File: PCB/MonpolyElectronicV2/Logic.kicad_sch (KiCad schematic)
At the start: 2 parts, among them J1 F51L-1A7H1-11020, U1 ESP32-S3-WROOM-1(N8R8)

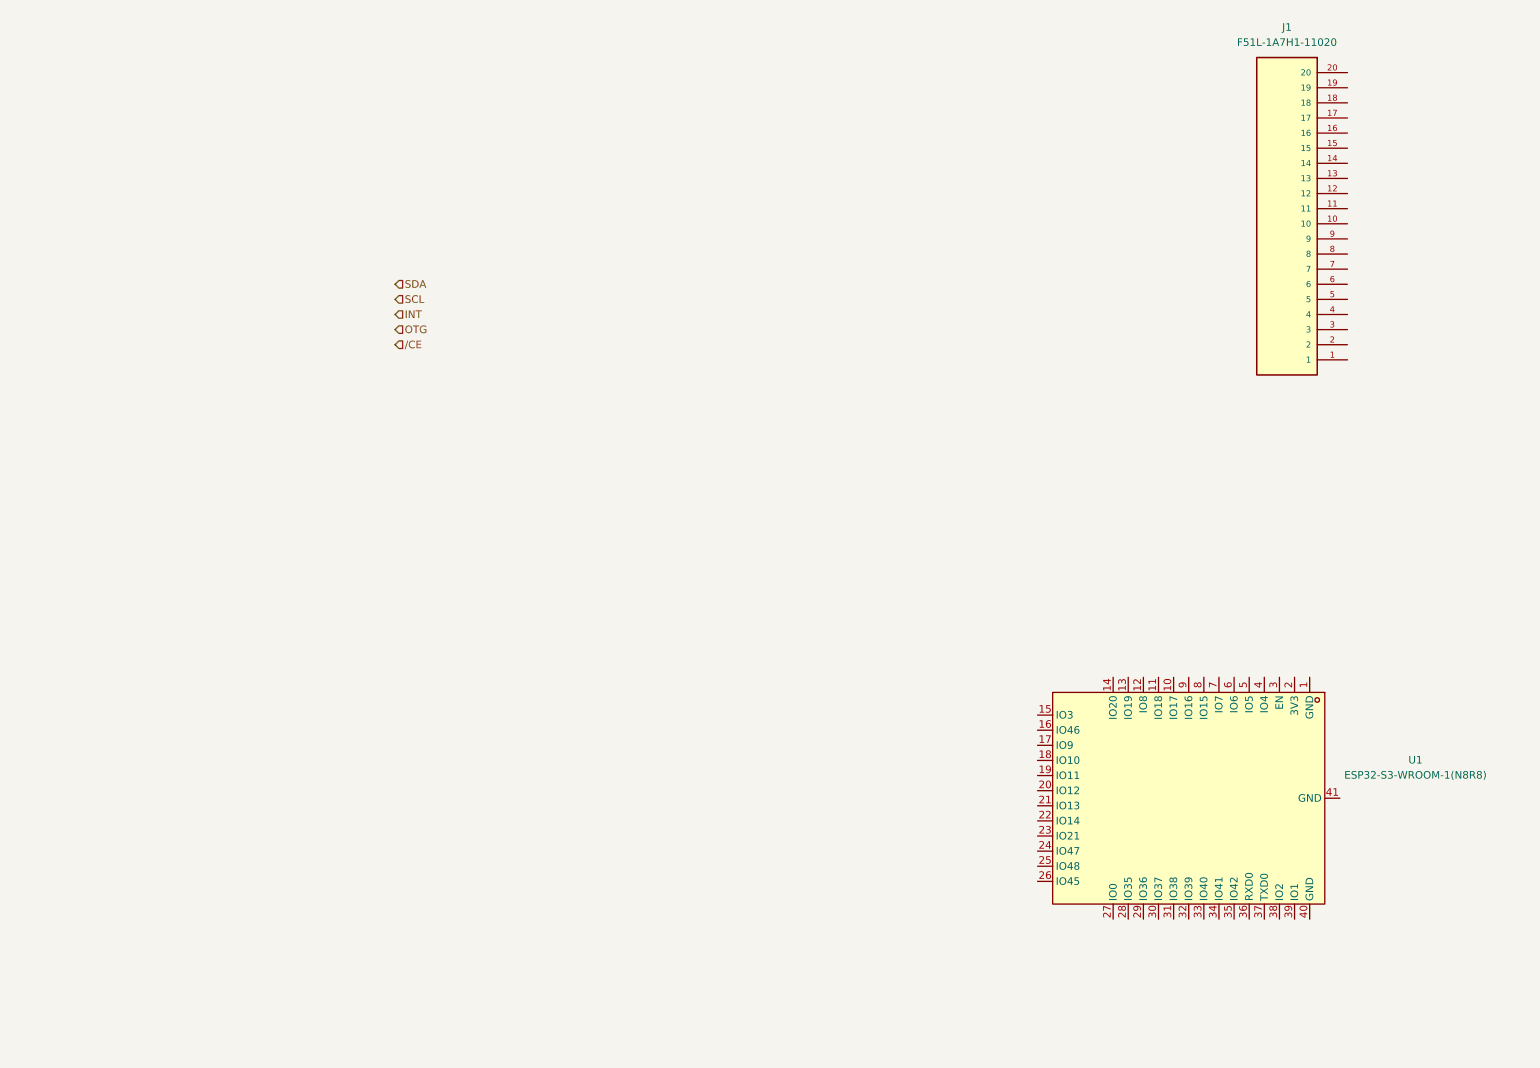
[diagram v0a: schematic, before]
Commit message: work on Logic part (MCU): audio done, programming done, ESP32 and inputs WIP, diplay not yet started
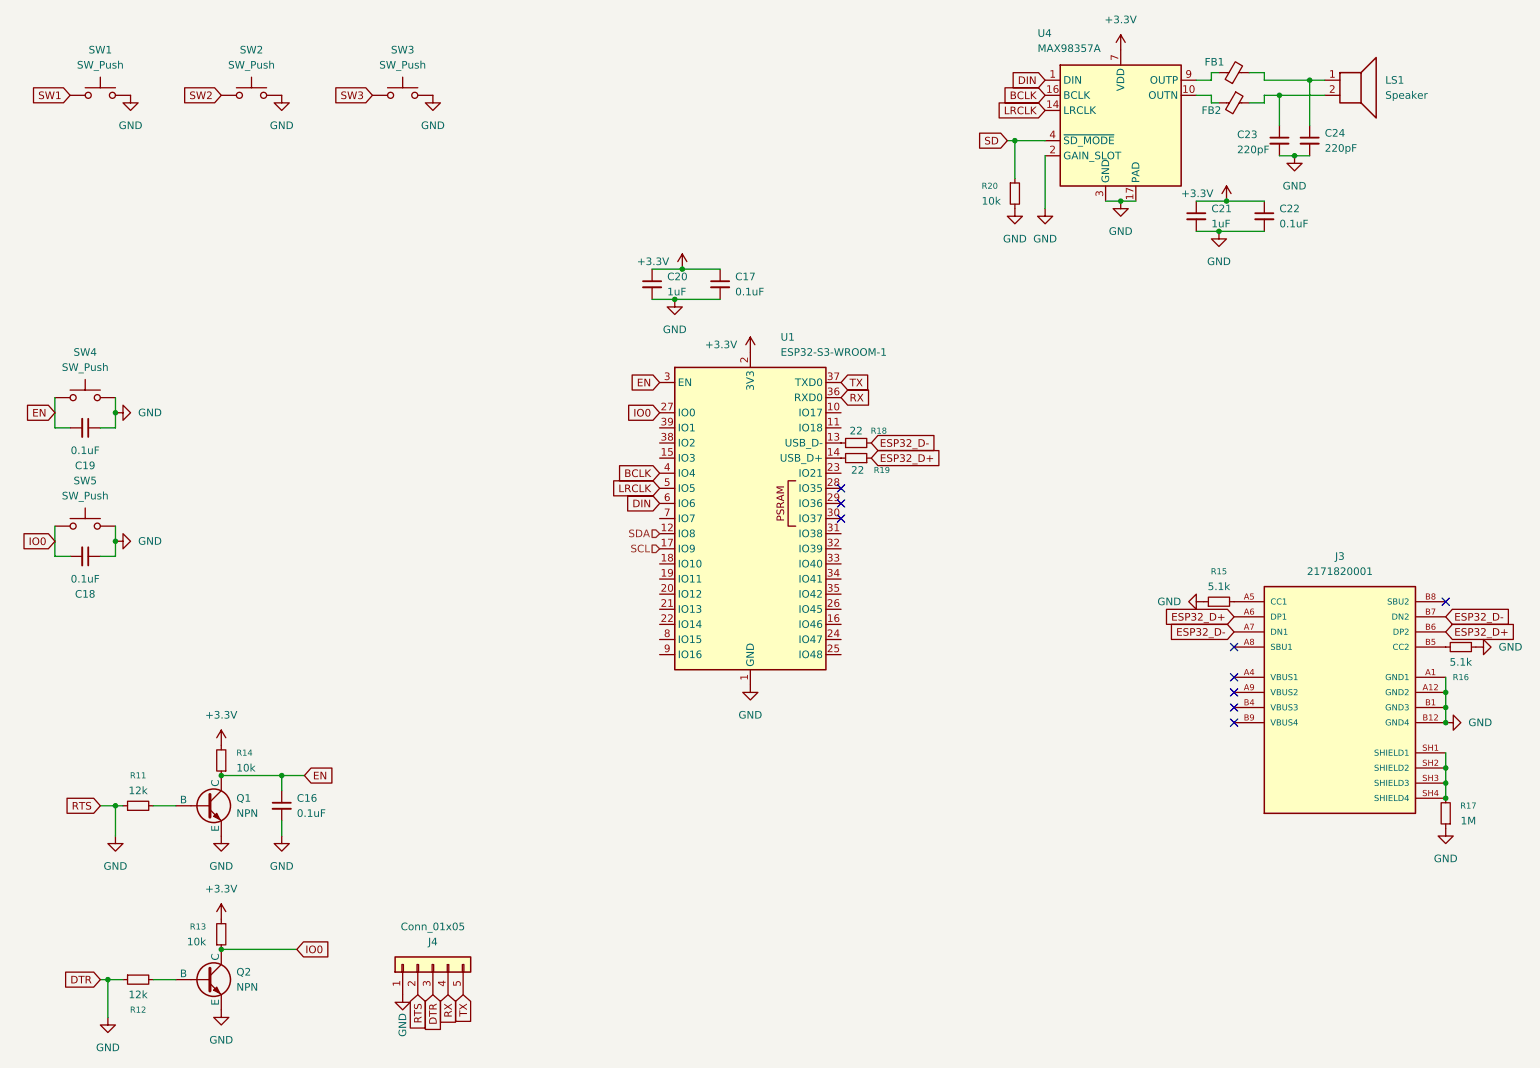
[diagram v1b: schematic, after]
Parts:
- removed J1: F51L-1A7H1-11020, Extra:AMPHENOL_F51L-1A7H1-11020, symbol Extra:F51L-1A7H1-11020
- removed U1: ESP32-S3-WROOM-1(N8R8), easyeda2kicad:WIRELM-SMD_ESP32-S3-WROOM-1, symbol easyeda2kicad:ESP32-S3-WROOM-1(N8R8)
- added C16, C17, C18, C19, C22: 0.1uF, symbol Device:C_Small
- added C20, C21: 1uF, symbol Device:C_Small
- added C23, C24: 220pF, symbol Device:C_Small
- added FB1, FB2: BLM21PG221SN1D, symbol Device:FerriteBead_Small
- added J3: 2171820001, Extra:MOLEX_2171820001, symbol Extra:2171820001
- added J4: Conn_01x05, symbol Connector_Generic:Conn_01x05
- added LS1: Speaker, symbol Device:Speaker
- added Q1, Q2: NPN, symbol Simulation_SPICE:NPN
- added R11, R12: 12k, symbol Device:R_Small
- added R13, R14, R20: 10k, symbol Device:R_Small
- added R15, R16: 5.1k, symbol Device:R_Small
- added R17: 1M, symbol Device:R_Small
- added R18, R19: 22, symbol Device:R_Small
- added SW1, SW2, SW3, SW4, SW5: SW_Push, symbol Switch:SW_Push
- added U1: ESP32-S3-WROOM-1, RF_Module:ESP32-S3-WROOM-1, symbol RF_Module:ESP32-S3-WROOM-1
- added U4: MAX98357A, Package_DFN_QFN:TQFN-16-1EP_3x3mm_P0.5mm_EP1.23x1.23mm, symbol Audio:MAX98357A
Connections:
- net SCL: now also U1.17 (IO9)
- net SDA: now also U1.12 (IO8)
- new net: R18.1, U1.13 (USB_D-)
- new net: J3.SH1 (SHIELD1), J3.SH2 (SHIELD2), J3.SH3 (SHIELD3), J3.SH4 (SHIELD4), R17.2
- new net: R19.2, U1.14 (USB_D+)
- new net: FB2.2, U4.10 (OUTN)
- new net: FB1.1, U4.9 (OUTP)
- new net: Q2.2 (B), R12.2
- new net: C24.1, FB1.2, LS1.1
- new net: C23.1, FB2.1, LS1.2
- new net: Q1.2 (B), R11.2
- new net: J3.B5 (CC2), R16.2
- new net: J3.A5 (CC1), R15.2
- new net +3.3V: C17.1, C20.1, C21.1, C22.1, R13.2, R14.2, U1.2 (3V3), U4.7 (VDD), U4.8 (VDD)
- new net BCLK: U1.4 (IO4), U4.16 (BCLK)
- new net DIN: U1.6 (IO6), U4.1 (DIN)
- new net EN: C16.1, C19.2, Q1.1 (C), R14.1, SW4.1, U1.3 (EN)
- new net ESP32_D+: J3.A6 (DP1), J3.B6 (DP2), R19.1
- new net ESP32_D-: J3.A7 (DN1), J3.B7 (DN2), R18.2
- new net GND: C16.2, C17.2, C18.1, C19.1, C20.2, C21.2, C22.2, C23.2, C24.2, J3.A1 (GND1), J3.A12 (GND2), J3.B1 (GND3), J3.B12 (GND4), J4.1 (Pin_1), J4.2 (Pin_2), J4.3 (Pin_3), Q1.3 (E), Q2.3 (E), R11.1, R12.1, R15.1, R16.1, R17.1, R20.2, SW1.2, SW2.2, SW3.2, SW4.2, SW5.2, U1.1 (GND), U1.40 (GND), U1.41 (GND), U4.11 (GND), U4.15 (GND), U4.17 (PAD), U4.2 (GAIN_SLOT), U4.3 (GND)
- new net IO0: C18.2, Q2.1 (C), R13.1, SW5.1, U1.27 (IO0)
- new net LRCLK: U1.5 (IO5), U4.14 (LRCLK)
- new net RX: J4.4 (Pin_4), U1.36 (RXD0)
- new net SD: R20.1, U4.4 (~{SD_MODE})
- new net SW1: SW1.1
- new net SW2: SW2.1
- new net SW3: SW3.1
- new net TX: J4.5 (Pin_5), U1.37 (TXD0)
- no-connect marks 0 -> 9

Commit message: find possible display
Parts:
- added C25, C26, C27: 0.1uF, symbol Device:C_Small
- added J1: Conn_01x14, symbol Connector_Generic:Conn_01x14
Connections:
- net +3.3V: now also J1.1 (Pin_1)
- net GND: now also C25.1, C26.1, C27.1, J1.2 (Pin_2)
- net SW1: now also C27.2
- net SW2: now also C26.2
- net SW3: now also C25.2
- net TFT_T_CS: now reaches U1.10 (IO17)
- net TFT_T_CS: now also J1.11 (Pin_11)
- net MOSI: now reaches U1.19 (IO11)
- net MOSI: now also J1.6 (Pin_6)
- net SCK: now reaches U1.20 (IO12)
- net SCK: now also J1.7 (Pin_7)
- net MISO: now reaches U1.21 (IO13)
- net MISO: now also J1.9 (Pin_9)
- net TFT_CS: now reaches U1.22 (IO14)
- net TFT_CS: now also J1.3 (Pin_3)
- net TFT_RESET: now reaches U1.8 (IO15)
- net TFT_RESET: now also J1.4 (Pin_4)
- net TFT_DC: now reaches U1.9 (IO16)
- net TFT_DC: now also J1.5 (Pin_5)
- new net TFT_IRQ: J1.14 (Pin_14)
- new net TFT_LED: J1.8 (Pin_8)
- new net TFT_T_CLK: J1.10 (Pin_10)
- new net TFT_T_DIN: J1.12 (Pin_12)
- new net TFT_T_DO: J1.13 (Pin_13)
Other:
- note added: "NFC!"

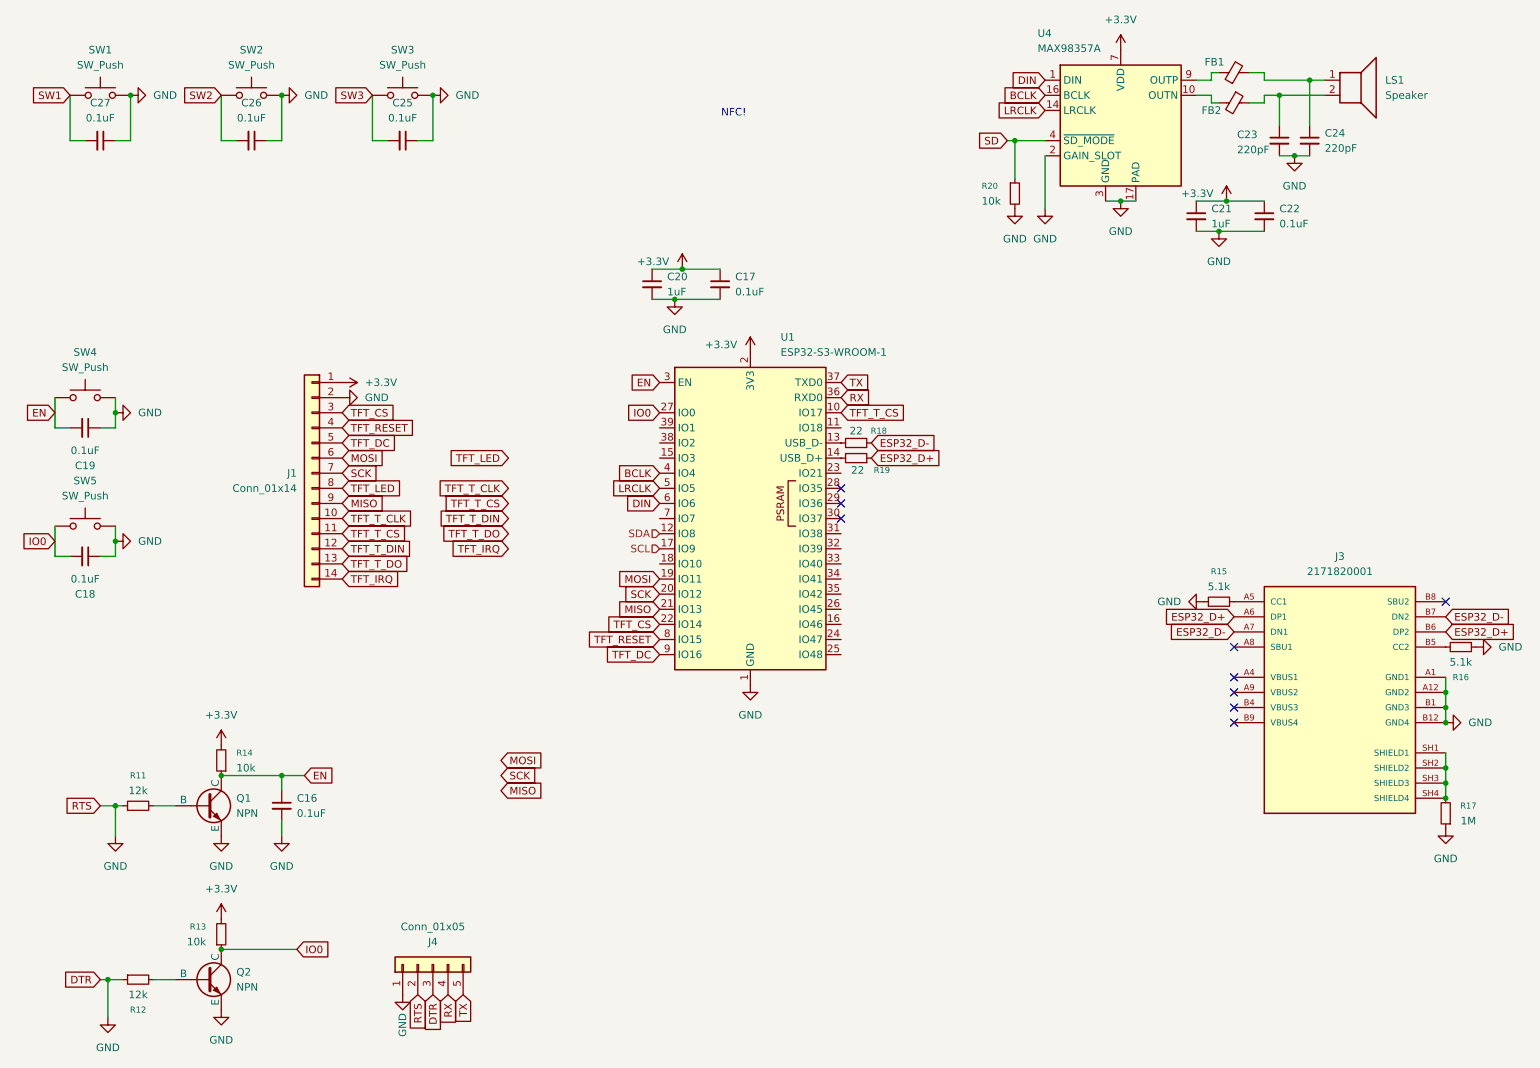
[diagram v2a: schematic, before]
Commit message: Finish Schematic wiring
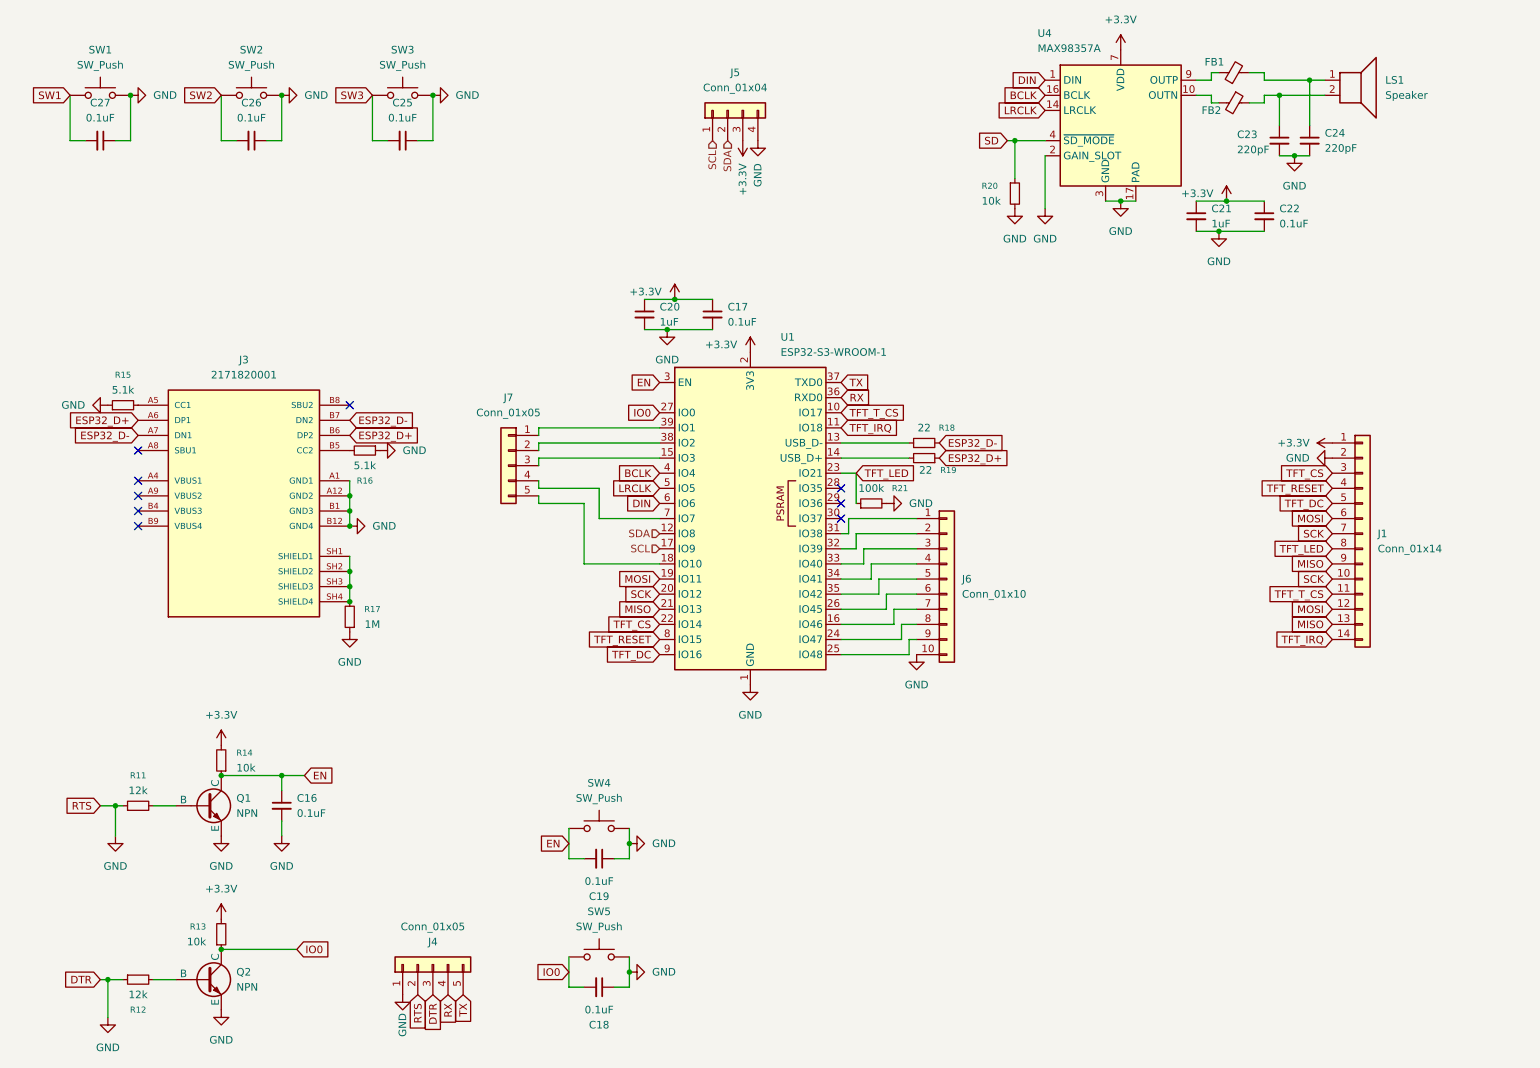
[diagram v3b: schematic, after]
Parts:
- added J5: Conn_01x04, symbol Connector_Generic:Conn_01x04
- added J6: Conn_01x10, symbol Connector_Generic:Conn_01x10
- added J7: Conn_01x05, symbol Connector_Generic:Conn_01x05
- added R21: 100k, symbol Device:R_Small
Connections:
- net TFT_T_CLK is gone; now on net SCK: J1.10 (Pin_10)
- net TFT_T_DIN is gone; now on net MOSI: J1.12 (Pin_12)
- net TFT_T_DO is gone; now on net MISO: J1.13 (Pin_13)
- net +3.3V: now also J5.3 (Pin_3)
- net GND: now also J5.4 (Pin_4), J6.10 (Pin_10), R21.2
- net SCL: now also J5.1 (Pin_1)
- net SDA: now also J5.2 (Pin_2)
- net TFT_IRQ: now also U1.11 (IO18)
- net TFT_LED: now also U1.23 (IO21), R21.1
- net at U1.15 (IO3): now also J7.3 (Pin_3)
- net at U1.16 (IO46): now also J6.7 (Pin_7)
- net at U1.18 (IO10): now also J7.5 (Pin_5)
- net at U1.24 (IO47): now also J6.8 (Pin_8)
- net at U1.25 (IO48): now also J6.9 (Pin_9)
- net at U1.26 (IO45): now also J6.6 (Pin_6)
- net at U1.31 (IO38): now also J6.1 (Pin_1)
- net at U1.32 (IO39): now also J6.2 (Pin_2)
- net at U1.33 (IO40): now also J6.3 (Pin_3)
- net at U1.34 (IO41): now also J6.4 (Pin_4)
- net at U1.35 (IO42): now also J6.5 (Pin_5)
- net at U1.38 (IO2): now also J7.2 (Pin_2)
- net at U1.39 (IO1): now also J7.1 (Pin_1)
- net at U1.7 (IO7): now also J7.4 (Pin_4)
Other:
- note removed: "NFC!"
- moved on the sheet: C17, C18, C19, C20, J1, J3, R15, R16, R17, R18, R19, SW4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

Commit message: Start adding footprints
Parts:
- C16, C17, C18, C19, C20, C21, C22, C25, C26, C27: footprint (none) -> Capacitor_SMD:C_0603_1608Metric
- FB1, FB2: footprint (none) -> Inductor_SMD:L_0805_2012Metric
- J1: footprint (none) -> Connector_PinHeader_2.54mm:PinHeader_1x14_P2.54mm_Vertical
- J4, J7: footprint (none) -> Connector_PinHeader_2.54mm:PinHeader_1x05_P2.54mm_Vertical
- J5: footprint (none) -> Connector_PinHeader_2.54mm:PinHeader_1x04_P2.54mm_Vertical
- J6: footprint (none) -> Connector_PinHeader_2.54mm:PinHeader_1x10_P2.54mm_Vertical
- LS1: footprint (none) -> Connector_JST:JST_XH_S2B-XH-A-1_1x02_P2.50mm_Horizontal
- Q1, Q2: footprint (none) -> Extra:SOT-23-231
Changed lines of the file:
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@@
 			)
 		)
-		(property "Footprint" ""
+		(property "Footprint" "Capacitor_SMD:C_0603_1608Metric"
 			(at 87.63 39.37 0)
 			(effects
@@
 			)
 		)
-		(property "Footprint" ""
+		(property "Footprint" "Capacitor_SMD:C_0603_1608Metric"
 			(at 120.65 181.61 0)
 			(effects
@@
 			)
 		)
-		(property "Footprint" ""
+		(property "Footprint" "Connector_PinHeader_2.54mm:PinHeader_1x10_P2.54mm_Vertical"
 			(at 179.07 113.03 0)
 			(effects
@@
 			)
 		)
-		(property "Footprint" ""
+		(property "Footprint" "Connector_PinHeader_2.54mm:PinHeader_1x05_P2.54mm_Vertical"
 			(at 92.71 177.8 0)
 			(effects
@@
 			)
 		)
-		(property "Footprint" ""
+		(property "Footprint" "Connector_PinHeader_2.54mm:PinHeader_1x04_P2.54mm_Vertical"
 			(at 142.24 34.29 0)
 			(effects
@@
 			)
 		)
-		(property "Footprint" ""
+		(property "Footprint" "Extra:SOT-23-231"
 			(at 118.11 180.34 0)
 			(effects
@@
 			)
 		)
-		(property "Footprint" ""
+		(property "Footprint" "Capacitor_SMD:C_0603_1608Metric"
 			(at 128.27 68.58 0)
 			(effects
@@
 			)
 		)
-		(property "Footprint" ""
+		(property "Footprint" "Capacitor_SMD:C_0603_1608Metric"
 			(at 120.65 160.02 0)
 			(effects
@@
 			)
 		)
-		(property "Footprint" ""
+		(property "Footprint" "Capacitor_SMD:C_0603_1608Metric"
 			(at 62.23 39.37 0)
 			(effects
@@
 			)
 		)
-		(property "Footprint" ""
+		(property "Footprint" "Connector_JST:JST_XH_S2B-XH-A-1_1x02_P2.50mm_Horizontal"
 			(at 247.65 34.29 0)
 			(effects
@@
 			)
 		)
-		(property "Footprint" ""
+		(property "Footprint" "Inductor_SMD:L_0805_2012Metric"
 			(at 227.33 29.718 90)
 			(effects
@@
 			)
 		)
-		(property "Footprint" ""
+		(property "Footprint" "Capacitor_SMD:C_0603_1608Metric"
 			(at 220.98 52.07 0)
 			(effects
@@
 			)
 		)
-		(property "Footprint" ""
+		(property "Footprint" "Capacitor_SMD:C_0603_1608Metric"
 			(at 232.41 52.07 0)
 			(effects
@@
 			)
 		)
-		(property "Footprint" ""
+		(property "Footprint" "Connector_PinHeader_2.54mm:PinHeader_1x05_P2.54mm_Vertical"
 			(at 105.41 93.98 0)
 			(effects
@@
 			)
 		)
-		(property "Footprint" ""
+		(property "Footprint" "Extra:SOT-23-231"
 			(at 118.11 151.13 0)
 			(effects
@@
 			)
 		)
-		(property "Footprint" ""
+		(property "Footprint" "Capacitor_SMD:C_0603_1608Metric"
 			(at 67.31 151.13 0)
 			(effects
@@
 			)
 		)
-		(property "Footprint" ""
+		(property "Footprint" "Connector_PinHeader_2.54mm:PinHeader_1x14_P2.54mm_Vertical"
 			(at 248.92 105.41 0)
 			(effects
@@
 			)
 		)
-		(property "Footprint" ""
+		(property "Footprint" "Inductor_SMD:L_0805_2012Metric"
 			(at 227.33 31.242 90)
 			(effects
@@
 			)
 		)
-		(property "Footprint" ""
+		(property "Footprint" "Capacitor_SMD:C_0603_1608Metric"
 			(at 36.83 39.37 0)
 			(effects
@@
 			)
 		)
-		(property "Footprint" ""
+		(property "Footprint" "Capacitor_SMD:C_0603_1608Metric"
 			(at 139.7 68.58 0)
 			(effects
